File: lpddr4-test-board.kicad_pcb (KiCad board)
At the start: 8 copper layers, 117 x 86 mm, 261 parts, among them IC1 TPS54561, IC2 NCP380HMUAJAATBG, IC3 TPD8S009DSMR, J1 0878311420, J2 08B0-1X1T-36-F, J3 DC_SOCKET, J4 WE_629105150521, J5 61300611121, J6 685119134923, J7 1140084168, J8 61300411121, J9 ddr3-sodimm-slot-2-2013289-2, Q1 BC817W, Q2 BSS138APW, Q3 BSS138APW, Q4 BSS138APW, Q5 BSS138APW, Q6 BSS138APW, U1 XC7K70T-FBG484, U10 REF3012AIDBZT, U12 FT2232HQ, U2 ASEM1-100.000MHZ-LC-T, U3 S25FL128SAGNFI000, U4 TPS65296, U5 TPS62823DLCT, U6 DP83848JSQ_NOPB, Y1 ABM8G-25.000MHZ-18-D2Y-T

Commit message: Update arrangement WiP
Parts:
- moved C184 2.95 mm to (134.4, 125.3)
- moved C185 2.95 mm to (132.4, 125.3)
- moved C186 2.95 mm to (137.4, 119.3)
- moved C187 2.95 mm to (135.4, 125.3)
- moved C188 2.95 mm to (131.9, 116.3)
- moved C189 2.95 mm to (133.4, 125.3)
- moved C190 2.95 mm to (132.4, 119.3)
- moved C191 2.95 mm to (131.4, 114.3)
- moved C192 2.95 mm to (133.4, 114.3)
- moved C193 2.95 mm to (133.4, 119.3)
- moved C194 2.95 mm to (137.4, 114.2)
- moved C195 2.95 mm to (132.4, 114.3)
- moved C196 2.95 mm to (136.4, 119.3)
- moved C197 2.95 mm to (131.4, 119.3)
- moved C198 2.95 mm to (136.4, 114.3)
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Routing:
- net SD_CD: track 21.9 -> 21.2 mm
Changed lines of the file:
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@@
     (thickness 1.6)
     (drawings 130)
-    (tracks 4521)
+    (tracks 4520)
     (zones 0)
     (modules 261)
@@
     (35 F.Paste user hide)
     (36 B.SilkS user hide)
-    (37 F.SilkS user hide)
+    (37 F.SilkS user)
     (38 B.Mask user hide)
     (39 F.Mask user hide)
@@
   )
   (module lpddr4-test-board-footprints:0402-res (layer B.Cu)
-    (at 132.468 118.883 270)
+    (at 135.389 119.264 270)
     (descr "Resistor SMD 0402 (1005 Metric), square (rectangular) end terminal, IPC_7351 nominal, (Body size source: http://www.tortai-tech.com/upload/download/2011102023233369053.pdf), generated with kicad-footprint-generator")
     (tags resistor)
@@
   )
   (module lpddr4-test-board-footprints:0402-res (layer B.Cu)
-    (at 131.468 118.883 270)
+    (at 134.389 119.264 270)
     (descr "Resistor SMD 0402 (1005 Metric), square (rectangular) end terminal, IPC_7351 nominal, (Body size source: http://www.tortai-tech.com/upload/download/2011102023233369053.pdf), generated with kicad-footprint-generator")
     (tags resistor)
@@
   )
   (module lpddr4-test-board-footprints:0603 (layer B.Cu)
-    (at 126.468 122.883)
+    (at 129.389 123.264)
     (attr smd)
     (fp_text reference FB6 (at 0 0 90) (layer F.SilkS) hide
@@
   )
   (module lpddr4-test-board-footprints:0603 (layer B.Cu)
-    (at 129.468 122.883)
+    (at 132.389 123.264)
     (attr smd)
     (fp_text reference FB5 (at 0 0 -90) (layer F.SilkS) hide
@@
   )
   (module lpddr4-test-board-footprints:0603 (layer B.Cu)
-    (at 132.468 122.883 180)
+    (at 135.389 123.264 180)
     (attr smd)
     (fp_text reference FB4 (at 0 0 -90) (layer F.SilkS) hide
@@
   )
   (module lpddr4-test-board-footprints:SOT-3 (layer F.Cu)
-    (at 131.05181 122.883)
+    (at 133.97281 123.264)
     (descr http://www.ti.com/lit/ds/symlink/tpd2eusb30.pdf)
     (attr smd)
@@
   )
   (module lpddr4-test-board-footprints:0402-cap (layer B.Cu)
-    (at 133.468 113.883 270)
+    (at 136.389 114.264 270)
     (descr "Resistor SMD 0402 (1005 Metric), square (rectangular) end terminal, IPC_7351 nominal, (Body size source: http://www.tortai-tech.com/upload/download/2011102023233369053.pdf), generated with kicad-footprint-generator")
     (tags resistor)
@@
   )
   (module lpddr4-test-board-footprints:0402-cap (layer B.Cu)
-    (at 128.468 118.883 90)
+    (at 131.389 119.264 90)
     (descr "Resistor SMD 0402 (1005 Metric), square (rectangular) end terminal, IPC_7351 nominal, (Body size source: http://www.tortai-tech.com/upload/download/2011102023233369053.pdf), generated with kicad-footprint-generator")
     (tags resistor)
@@
   )
   (module lpddr4-test-board-footprints:0402-cap (layer B.Cu)
-    (at 133.468 118.883 90)
+    (at 136.389 119.264 90)
     (descr "Resistor SMD 0402 (1005 Metric), square (rectangular) end terminal, IPC_7351 nominal, (Body size source: http://www.tortai-tech.com/upload/download/2011102023233369053.pdf), generated with kicad-footprint-generator")
     (tags resistor)
@@
   )
   (module lpddr4-test-board-footprints:0402-cap (layer B.Cu)
-    (at 129.468 113.883 270)
+    (at 132.389 114.264 270)
     (descr "Resistor SMD 0402 (1005 Metric), square (rectangular) end terminal, IPC_7351 nominal, (Body size source: http://www.tortai-tech.com/upload/download/2011102023233369053.pdf), generated with kicad-footprint-generator")
     (tags resistor)
@@
   )
   (module lpddr4-test-board-footprints:0402-cap (layer B.Cu)
-    (at 134.468 113.868 270)
+    (at 137.389 114.249 270)
     (descr "Resistor SMD 0402 (1005 Metric), square (rectangular) end terminal, IPC_7351 nominal, (Body size source: http://www.tortai-tech.com/upload/download/2011102023233369053.pdf), generated with kicad-footprint-generator")
     (tags resistor)
@@
   )
   (module lpddr4-test-board-footprints:0402-cap (layer B.Cu)
-    (at 130.468 118.883 90)
+    (at 133.389 119.264 90)
     (descr "Resistor SMD 0402 (1005 Metric), square (rectangular) end terminal, IPC_7351 nominal, (Body size source: http://www.tortai-tech.com/upload/download/2011102023233369053.pdf), generated with kicad-footprint-generator")
     (tags resistor)
@@
   )
   (module lpddr4-test-board-footprints:0402-cap (layer B.Cu)
-    (at 130.468 113.883 270)
+    (at 133.389 114.264 270)
     (descr "Resistor SMD 0402 (1005 Metric), square (rectangular) end terminal, IPC_7351 nominal, (Body size source: http://www.tortai-tech.com/upload/download/2011102023233369053.pdf), generated with kicad-footprint-generator")
     (tags resistor)
@@
   )
   (module lpddr4-test-board-footprints:0402-cap (layer B.Cu)
-    (at 128.468 113.883 270)
+    (at 131.389 114.264 270)
     (descr "Resistor SMD 0402 (1005 Metric), square (rectangular) end terminal, IPC_7351 nominal, (Body size source: http://www.tortai-tech.com/upload/download/2011102023233369053.pdf), generated with kicad-footprint-generator")
     (tags resistor)
@@
   )
   (module lpddr4-test-board-footprints:0402-cap (layer B.Cu)
-    (at 129.468 118.883 90)
+    (at 132.389 119.264 90)
     (descr "Resistor SMD 0402 (1005 Metric), square (rectangular) end terminal, IPC_7351 nominal, (Body size source: http://www.tortai-tech.com/upload/download/2011102023233369053.pdf), generated with kicad-footprint-generator")
     (tags resistor)
@@
   )
   (module lpddr4-test-board-footprints:0402-cap (layer B.Cu)
-    (at 130.468 124.883 270)
+    (at 133.389 125.264 270)
     (descr "Resistor SMD 0402 (1005 Metric), square (rectangular) end terminal, IPC_7351 nominal, (Body size source: http://www.tortai-tech.com/upload/download/2011102023233369053.pdf), generated with kicad-footprint-generator")
     (tags resistor)
@@
   )
   (module lpddr4-test-board-footprints:0402-cap (layer B.Cu)
-    (at 128.968 115.883)
+    (at 131.889 116.264)
     (descr "Resistor SMD 0402 (1005 Metric), square (rectangular) end terminal, IPC_7351 nominal, (Body size source: http://www.tortai-tech.com/upload/download/2011102023233369053.pdf), generated with kicad-footprint-generator")
     (tags resistor)
@@
   )
   (module lpddr4-test-board-footprints:0402-cap (layer B.Cu)
-    (at 132.468 124.883 270)
+    (at 135.389 125.264 270)
     (descr "Resistor SMD 0402 (1005 Metric), square (rectangular) end terminal, IPC_7351 nominal, (Body size source: http://www.tortai-tech.com/upload/download/2011102023233369053.pdf), generated with kicad-footprint-generator")
     (tags resistor)
@@
   )
   (module lpddr4-test-board-footprints:0402-cap (layer B.Cu)
-    (at 134.468 118.883 90)
+    (at 137.389 119.264 90)
     (descr "Resistor SMD 0402 (1005 Metric), square (rectangular) end terminal, IPC_7351 nominal, (Body size source: http://www.tortai-tech.com/upload/download/2011102023233369053.pdf), generated with kicad-footprint-generator")
     (tags resistor)
@@
   )
   (module lpddr4-test-board-footprints:0402-cap (layer B.Cu)
-    (at 129.468 124.883 270)
+    (at 132.389 125.264 270)
     (descr "Resistor SMD 0402 (1005 Metric), square (rectangular) end terminal, IPC_7351 nominal, (Body size source: http://www.tortai-tech.com/upload/download/2011102023233369053.pdf), generated with kicad-footprint-generator")
     (tags resistor)
@@
   )
   (module lpddr4-test-board-footprints:0402-cap (layer B.Cu)
-    (at 131.468 124.883 270)
+    (at 134.389 125.264 270)
     (descr "Resistor SMD 0402 (1005 Metric), square (rectangular) end terminal, IPC_7351 nominal, (Body size source: http://www.tortai-tech.com/upload/download/2011102023233369053.pdf), generated with kicad-footprint-generator")
     (tags resistor)
@@
   )
   (module lpddr4-test-board-footprints:BEL_08B0-1X1T-36-F (layer F.Cu)
-    (at 198.648 123.986 180)
+    (at 200.807 123.986 180)
     (fp_text reference J2 (at -4.176 17.3154) (layer F.SilkS)
       (effects (font (size 1.514331 1.514331) (thickness 0.015)))
@@
   )
   (module lpddr4-test-board-footprints:QFN50P900X900X100-65N (layer F.Cu)
-    (at 131.468 116.383 90)
+    (at 134.389 116.764 90)
     (fp_text reference U12 (at -2.12661 -5.88945 90) (layer F.SilkS)
       (effects (font (size 1.000756 1.000756) (thickness 0.015)))
@@
   )
   (module lpddr4-test-board-footprints:USB_Micro_B_Female_629105150521 (layer F.Cu)
-    (at 131.211 131.098)
+    (at 134.132 131.479)
     (descr "USB Micro-B receptacle, http://www.mouser.com/ds/2/445/629105150521-469306.pdf")
     (tags "usb micro receptacle")
@@
   (segment (start 173.536329 108.497157) (end 173.507157 108.497157) (width 0.15) (layer F.Cu) (net 539))
   (segment (start 173.507157 108.497157) (end 173.502 108.492) (width 0.15) (layer F.Cu) (net 539))
-  (segment (start 173.502 108.492) (end 172.994 109) (width 0.15) (layer B.Cu) (net 533))
   (segment (start 178.836 124.598) (end 177.693 124.598) (width 0.15) (layer F.Cu) (net 533))
   (via (at 176.931 124.621) (size 0.5) (drill 0.2) (layers F.Cu B.Cu) (net 533))

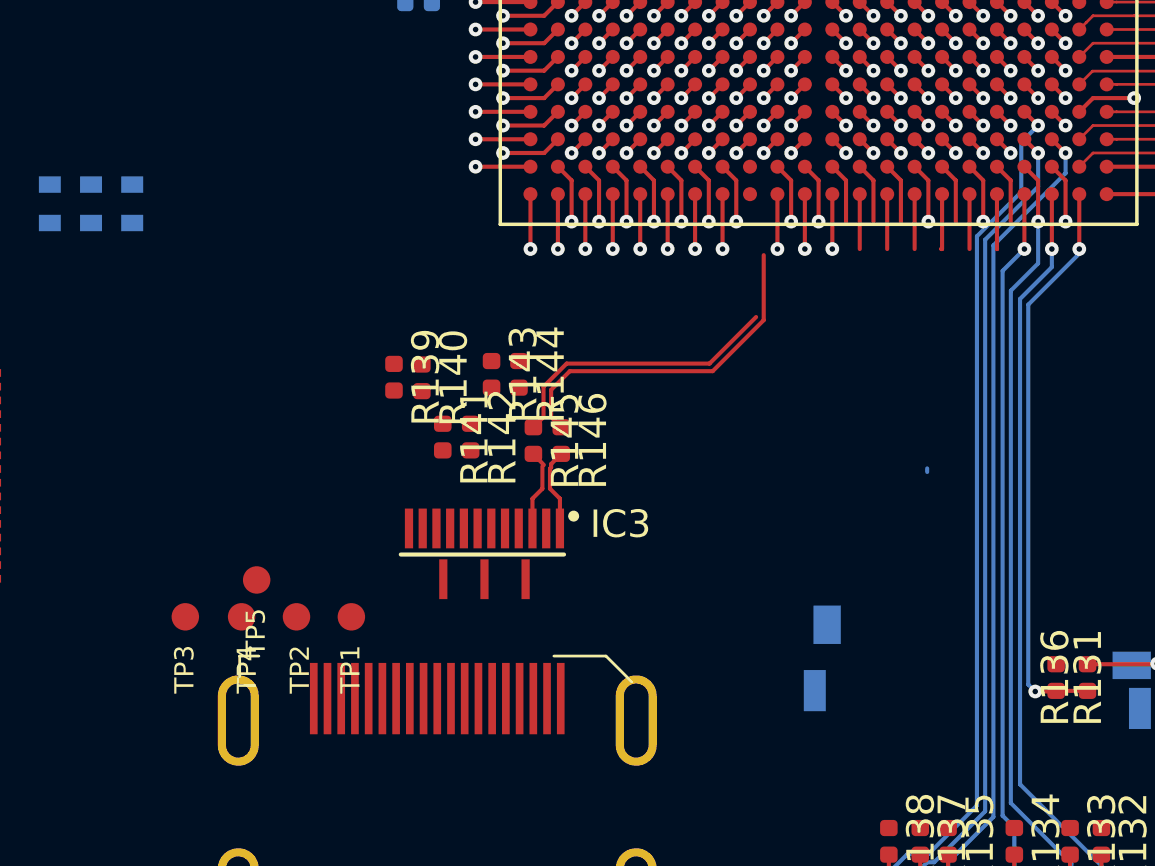
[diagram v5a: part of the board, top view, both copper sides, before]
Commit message: Add HDMI routing
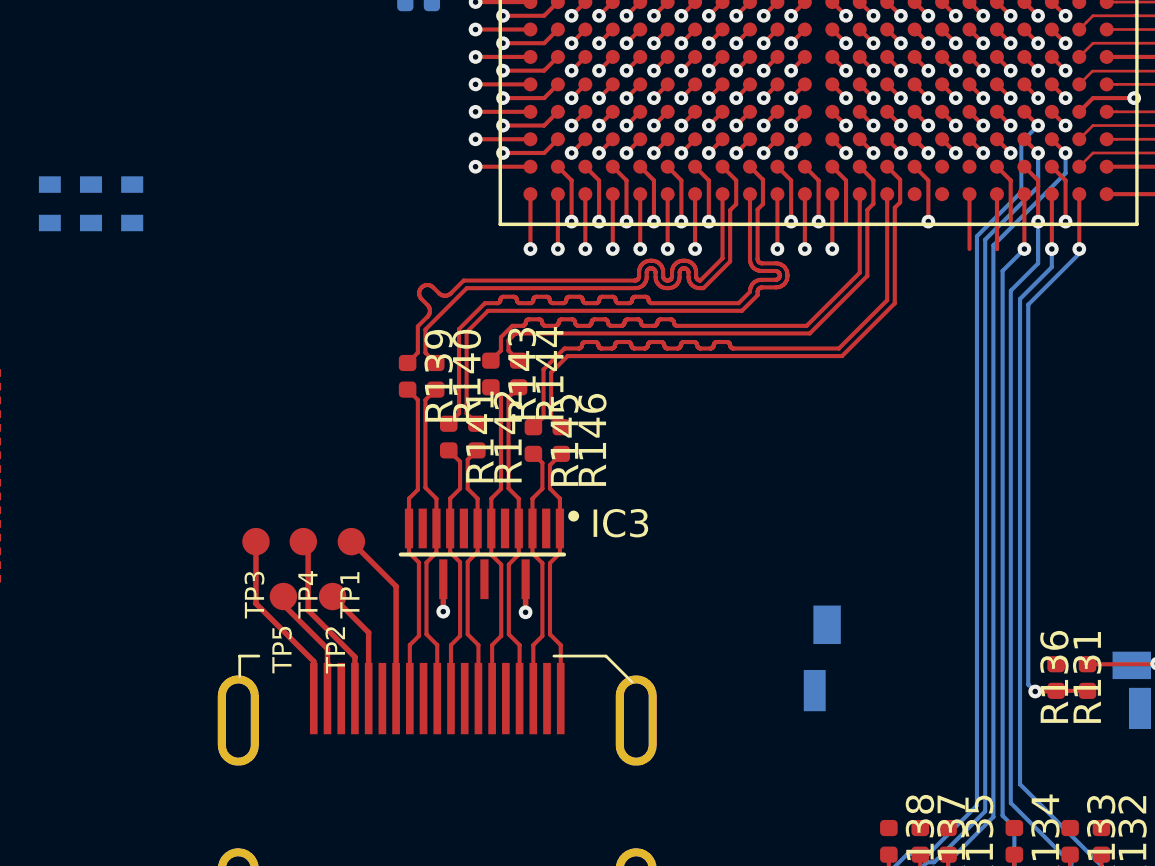
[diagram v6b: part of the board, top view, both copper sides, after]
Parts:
- moved TP3 3.76 mm to (148.6, 119.2)
- moved TP4 3.54 mm to (150.5, 119.2)
- moved TP1 2.74 mm to (152.1, 119.2)
- moved TP2 1.51 mm to (151.5, 121.2)
- moved TP5 1.15 mm to (149.6, 121.2)
- moved R140 0.51 mm to (155.1, 113.1)
- moved R139 0.50 mm to (154.1, 113.1)
- moved R142 0.23 mm to (156.6, 115.3)
- moved R141 0.22 mm to (155.6, 115.3)
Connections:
- U1 pad J21: Net-(U1-PadJ21) -> TMDS_D2_P
- U1 pad J22: Net-(U1-PadJ22) -> TMDS_D2_N
- U1 pad K21: Net-(U1-PadK21) -> TMDS_D1_P
- U1 pad K22: Net-(U1-PadK22) -> TMDS_D1_N
- U1 pad P21: TMDS_D2_P -> TMDS_D0_P
- U1 pad P22: TMDS_D2_N -> TMDS_D0_N
- U1 pad R21: TMDS_D1_P -> TMDS_CLK_P
- U1 pad R22: TMDS_D1_N -> TMDS_CLK_N
- U1 pad U21: TMDS_D0_N -> Net-(U1-PadU21)
- U1 pad U22: TMDS_D0_P -> Net-(U1-PadU22)
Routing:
- net TMDS_D0_P: track 2.00 -> 21.3 mm, vias 1 -> 0
- net TMDS_CLK_N: track 0.00 -> 19.2 mm
- net TMDS_CLK_P: track 0.00 -> 19.2 mm
- net TMDS_D0_N: track 2.21 -> 21.4 mm, vias 1 -> 0
- net TMDS_D1_N: track 2.00 -> 19.3 mm, vias 1 -> 0
- net TMDS_D1_P: track 2.21 -> 19.2 mm, vias 1 -> 0
- net C_TMDS_D1_P: track 0.00 -> 12.0 mm
- net C_TMDS_D1_N: track 0.00 -> 11.9 mm
- net C_TMDS_CLK_P: track 0.00 -> 11.9 mm
- net C_TMDS_CLK_N: track 0.00 -> 11.8 mm
- net TMDS_D2_N: track 10.4 -> 21.0 mm
- net C_TMDS_D0_N: track 0.00 -> 9.65 mm
- net C_TMDS_D0_P: track 0.00 -> 9.65 mm
- net TMDS_D2_P: track 12.7 -> 21.0 mm
- net Net-(J6-Pad19): track 0.00 -> 6.59 mm
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
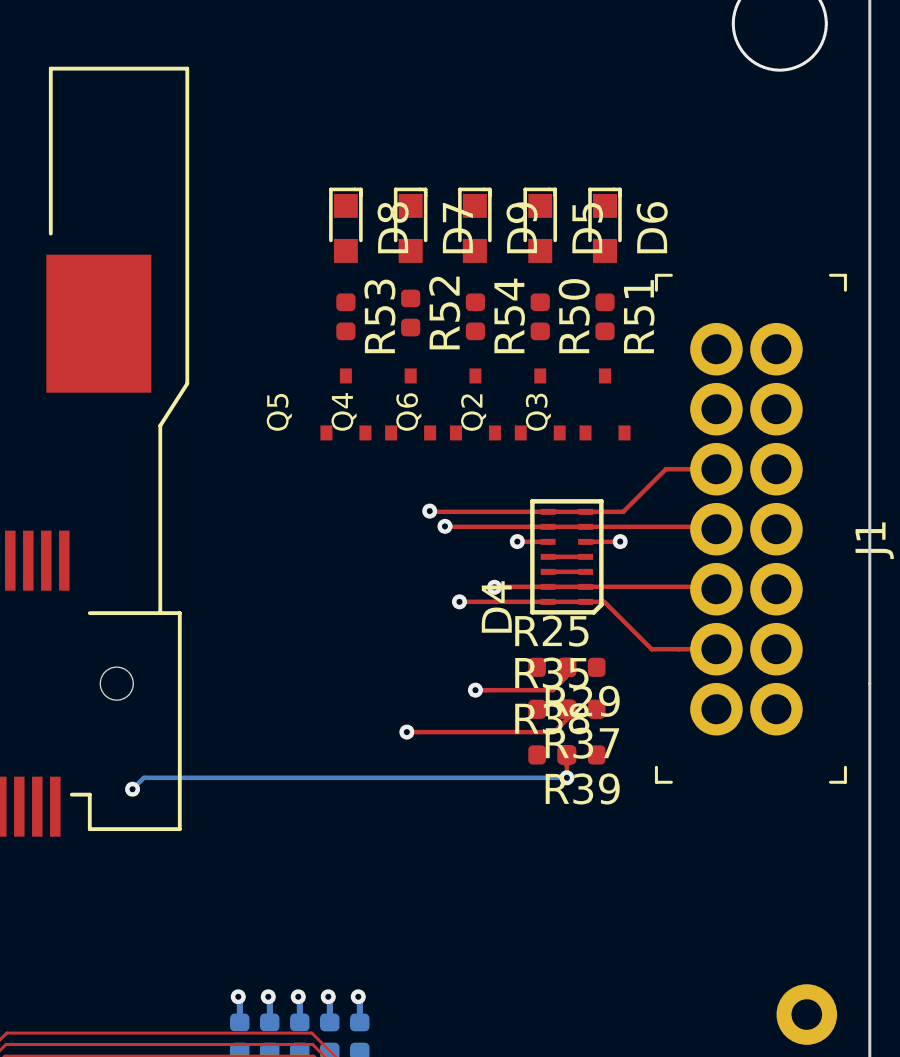
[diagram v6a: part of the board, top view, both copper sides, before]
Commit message: Route USR LEDs
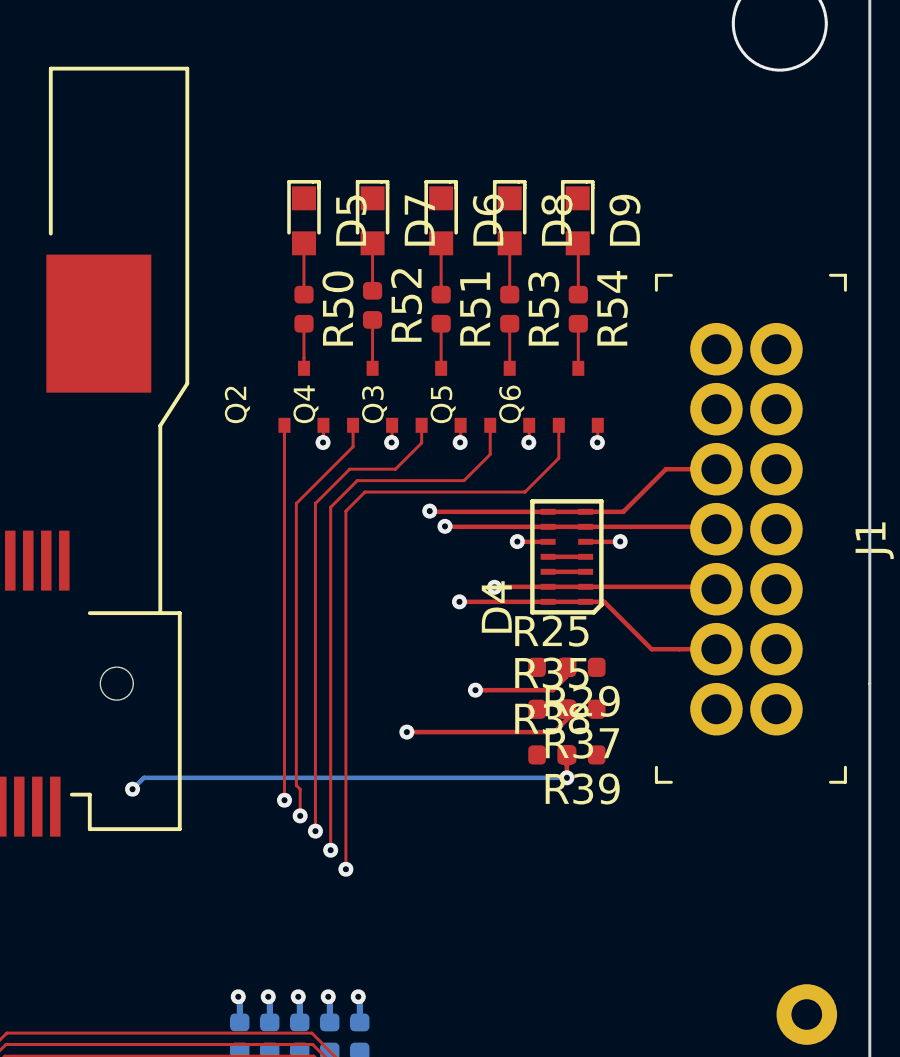
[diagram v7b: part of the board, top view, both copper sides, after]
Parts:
- moved D5 7.88 mm to (198.1, 59.6)
- moved Q2 7.88 mm to (198.1, 65.4)
- moved R50 7.88 mm to (198.1, 62.5)
- moved Q3 5.47 mm to (202.7, 65.4)
- moved D6 5.47 mm to (202.7, 59.6)
- moved R51 5.47 mm to (202.7, 62.5)
- moved Q5 5.47 mm to (205.0, 65.4)
- moved D8 5.47 mm to (205.0, 59.6)
- moved R53 5.47 mm to (205.0, 62.5)
- moved Q6 3.44 mm to (207.3, 65.4)
- moved R54 3.44 mm to (207.3, 62.5)
- moved D9 3.44 mm to (207.3, 59.6)
- moved Q4 1.30 mm to (200.4, 65.4)
- moved R52 1.30 mm to (200.4, 62.4)
- moved D7 1.30 mm to (200.4, 59.6)
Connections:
- U1 pad A8: Net-(U1-PadA8) -> USR_LED5
- U1 pad B8: Net-(U1-PadB8) -> USR_LED4
- U1 pad C8: Net-(U1-PadC8) -> USR_LED3
- U1 pad E8: Net-(U1-PadE8) -> USR_LED2
- U1 pad F8: Net-(U1-PadF8) -> USR_LED1
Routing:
- net USR_LED5: track 0.00 -> 45.5 mm, vias 0 -> 2
- net USR_LED4: track 0.00 -> 43.9 mm, vias 0 -> 2
- net USR_LED3: track 0.00 -> 42.1 mm, vias 0 -> 2
- net USR_LED2: track 0.00 -> 41.8 mm, vias 0 -> 2
- net USR_LED1: track 0.00 -> 41.1 mm, vias 0 -> 2
- net GND: track 217.8 -> 220.7 mm, vias 182 -> 187
- net Net-(U1-PadB8): track 2.21 -> 0.00 mm, vias 1 -> 0
- net Net-(U1-PadA8): track 2.00 -> 0.00 mm, vias 1 -> 0
- net Net-(D9-Pad2): track 0.00 -> 1.72 mm
- net Net-(D8-Pad2): track 0.00 -> 1.71 mm
- net Net-(D6-Pad2): track 0.00 -> 1.71 mm
- net Net-(D5-Pad2): track 0.00 -> 1.71 mm
- net Net-(Q4-Pad3): track 0.00 -> 1.61 mm
- net Net-(D7-Pad2): track 0.00 -> 1.58 mm
- net Net-(Q6-Pad3): track 0.00 -> 1.49 mm
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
